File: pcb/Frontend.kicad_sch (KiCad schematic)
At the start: 382 parts, among them IC1 TS3021ILT, IC10 TS3021ILT, IC11 TS3021ILT, IC12 TS3021ILT, IC13 TS3021ILT, IC14 TS3021ILT, IC2 TS3021ILT, IC3 TS3021ILT, IC4 TS3021ILT, IC5 TS3021ILT, IC6 TS3021ILT, IC7 TS3021ILT, IC8 TS3021ILT, IC9 TS3021ILT, J1 Conn_01x05_Socket, J2 Conn_01x05_Socket, J3 Conn_01x04_Socket, J4 Conn_01x04_Socket, U1 TEA1-0505, U10 ADuM1400xRW, U11 GAQY212GS, U12 GAQY212GS, U13 GAQY212GS, U14 GAQY212GS, U15 LM4040DBZ-5, U16 DAC7311xDCK, U17 ADuM1300xRW, U18 TEA1-0505, U19 GAQY212GS, U2 GAQY212GS, U20 GAQY212GS, U21 GAQY212GS, U22 GAQY212GS, U23 GAQY212GS, U24 GAQY212GS, U25 GAQY212GS, U26 GAQY212GS, U27 ADuM1400xRW, U28 GAQY212GS, U29 GAQY212GS, U3 GAQY212GS, U30 GAQY212GS, U31 GAQY212GS, U32 LM4040DBZ-5, U33 DAC7311xDCK, U34 ADuM1300xRW, U35 TEA1-0505, U36 GAQY212GS, U37 GAQY212GS, U38 GAQY212GS, U39 GAQY212GS, U4 GAQY212GS, U40 GAQY212GS, U41 GAQY212GS, U42 ADuM1300xRW, U43 GAQY212GS, U44 GAQY212GS, U45 GAQY212GS, U46 LM4040DBZ-5, U47 DAC7311xDCK, U48 ADuM1300xRW, U49 TEA1-0505, U5 GAQY212GS, U50 GAQY212GS, U51 GAQY212GS, U52 GAQY212GS, U53 GAQY212GS, U54 GAQY212GS, U55 GAQY212GS, U56 ADuM1300xRW, U57 GAQY212GS, U58 GAQY212GS, U59 GAQY212GS, U6 GAQY212GS, U60 LM4040DBZ-5, U61 DAC7311xDCK, U62 ADuM1300xRW, U7 GAQY212GS, U8 GAQY212GS, U9 GAQY212GS

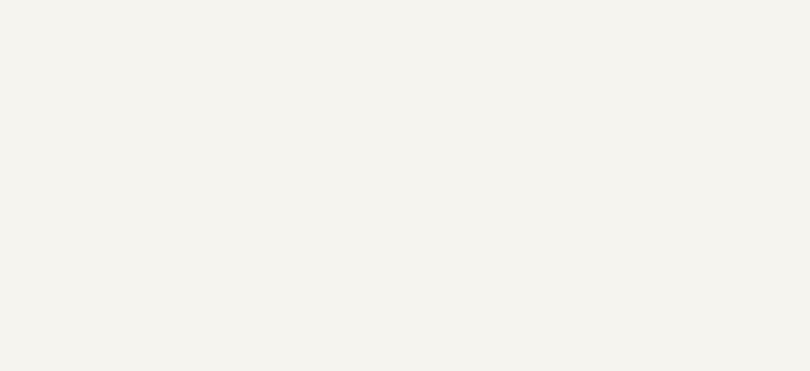
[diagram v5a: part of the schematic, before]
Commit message: Update TS3021ILT part and more routing
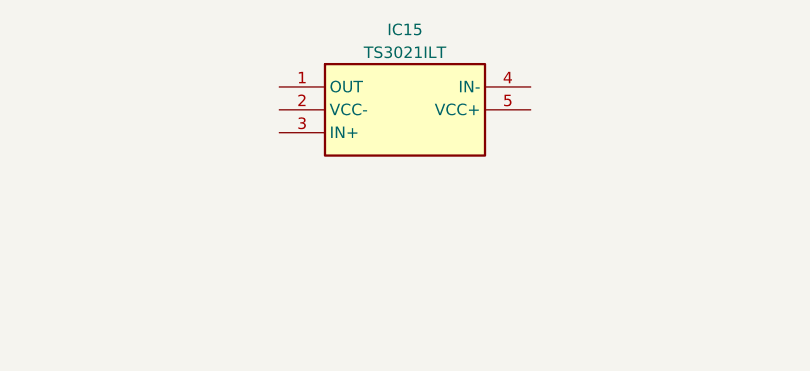
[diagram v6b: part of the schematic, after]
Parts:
- added IC15: TS3021ILT, SOT95P280X145-5N, symbol SamacSys_Parts:TS3021ILT
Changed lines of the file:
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@@
+	)
+	(symbol
+		(lib_id "SamacSys_Parts:TS3021ILT")
+		(at 457.2 -11.43 0)
+		(unit 1)
+		(exclude_from_sim no)
+		(in_bom yes)
+		(on_board yes)
+		(dnp no)
+		(fields_autoplaced yes)
+		(property "Reference" "IC15"
+			(at 471.17 -17.78 0)
+			(effects
+				(font
+					(size 1.27 1.27)
+				)
+			)
+		)
+		(property "Value" "TS3021ILT"
+			(at 471.17 -15.24 0)
+			(effects
+				(font
+					(size 1.27 1.27)
+				)
+			)
+		)
+		(property "Footprint" "SOT95P280X145-5N"
+			(at 481.33 83.49 0)
+			(effects
+				(font
+					(size 1.27 1.27)
+				)
+				(justify left top)
+				(hide yes)
+			)
+		)
+		(property "Datasheet" "https://www.st.com/resource/en/datasheet/ts3021.pdf"
+			(at 481.33 183.49 0)
+			(effects
+				(font
+					(size 1.27 1.27)
+				)
+				(justify left top)
+				(hide yes)
+			)
+		)
+		(property "Description" "Rail-to-rail 1.8 V high-speed comparator"
+			(at 457.2 -11.43 0)
+			(effects
+				(font
+					(size 1.27 1.27)
+				)
+				(hide yes)
+			)
+		)
+		(property "Height" "1.45"
+			(at 481.33 383.49 0)
+			(effects
+				(font
+					(size 1.27 1.27)
+				)
+				(justify left top)
+				(hide yes)
+			)
+		)
+		(property "TME Electronic Components Part Number" ""
+			(at 481.33 483.49 0)
+			(effects
+				(font
+					(size 1.27 1.27)
+				)
+				(justify left top)
+				(hide yes)
+			)
+		)
+		(property "TME Electronic Components Price/Stock" ""
+			(at 481.33 583.49 0)
+			(effects
+				(font
+					(size 1.27 1.27)
+				)
+				(justify left top)
+				(hide yes)
+			)
+		)
+		(property "Manufacturer_Name" "STMicroelectronics"
+			(at 481.33 683.49 0)
+			(effects
+				(font
+					(size 1.27 1.27)
+				)
+				(justify left top)
+				(hide yes)
+			)
+		)
+		(property "Manufacturer_Part_Number" "TS3021ILT"
+			(at 481.33 783.49 0)
+			(effects
+				(font
+					(size 1.27 1.27)
+				)
+				(justify left top)
+				(hide yes)
+			)
+		)
+		(pin "1"
+		)
+		(pin "3"
+		)
+		(pin "5"
+		)
+		(pin "4"
+		)
+		(pin "2"
+		)
+		(instances
+			(project ""
+				(path "/0c4edb77-9bdf-4103-be66-c5eb9940b163/92da3f15-6ca3-419e-9376-1f5f82193d40"
+					(reference "IC15")
+					(unit 1)
+				)
+			)
+		)
 	)
 	(symbol

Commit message: Update schematic, more routing
Add firmware/TSC_RangeControl.ioc (STM32CubeMX project for STM32C011F4Px). Numerous adjustments to the schematic. Update PCB files.
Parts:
- removed IC15: TS3021ILT, SOT95P280X145-5N, symbol SamacSys_Parts:TS3021ILT
- added C64, C65: 100n, Capacitor_SMD:C_0603_1608Metric, symbol Device:C
- added IC15: NCP51460SN33T1G, SOT96P237X111-3N, symbol SamacSys_Parts:NCP51460SN33T1G
- added U64: STM32C011F4Px, Package_SO:TSSOP-20_4.4x6.5mm_P0.65mm, symbol MCU_ST_STM32C0:STM32C011F4Px
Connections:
- net +5V: now also C65.1, IC15.1 (VIN)
- net GND: now also C64.2, C65.2, IC15.3 (GND), U64.5 (VSS)
- net at C48.1, C49.2, C52.2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: now also C58.2
- net at C17.1, C18.2, C21.2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: now also C28.2
- net at C1.1, C10.2, C11.2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: now also C12.2
- net at C12.1, FB10.1, U17.10 (V_{E2})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: no longer C12.2
- net at C58.1, FB29.1, U62.10 (V_{E2})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: no longer C58.2
- net at C28.1, FB17.1, U34.10 (V_{E2})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: no longer C28.2
- new net: C64.1, IC15.2 (VOUT), U64.4 (VDD)

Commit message: New range control concept
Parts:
- added C66, C67, C68, C69, C70, C71: 100n, Capacitor_SMD:C_0603_1608Metric, symbol Device:C
- added D15, D16, D17, D18: D, Diode_SMD:D_SOD-323F, symbol Device:D
- added IC16, IC17, IC18: NCP51460SN33T1G, Package_TO_SOT_SMD:SOT-23, symbol SamacSys_Parts:NCP51460SN33T1G
- added R201, R202, R203, R204: 10k, Resistor_SMD:R_0603_1608Metric, symbol Device:R
- added TP1, TP10, TP11, TP12, TP2, TP3, TP4, TP5, TP6, TP7, TP8, TP9: TestPoint, TestPoint:TestPoint_Pad_D1.0mm, symbol Connector:TestPoint
- added U65, U66, U67: STM32C011F4Px, Package_SO:TSSOP-20_4.4x6.5mm_P0.65mm, symbol MCU_ST_STM32C0:STM32C011F4Px
- IC15: footprint SOT96P237X111-3N -> Package_TO_SOT_SMD:SOT-23
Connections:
- net +5V: now also C67.1, C69.1, C71.1, IC16.1 (VIN), IC17.1 (VIN), IC18.1 (VIN)
- net CH1_IN1_R15: now also U64.8 (PA1)
- net CH1_IN1_R25: now also U64.9 (PA2)
- net CH1_IN1_R5: now also U64.7 (PA0)
- net CH1_IN2_R15: now also U64.11 (PA4)
- net CH1_IN2_R25: now also U64.12 (PA5)
- net CH1_IN2_R5: now also U64.10 (PA3)
- net CH1_IN3_R15: now also U64.14 (PA7)
- net CH1_IN3_R25: now also U64.15 (PA8)
- net CH1_IN3_R5: now also U64.13 (PA6)
- net CH1_IN4_R15: now also U64.17 (PA10/PA12)
- net CH1_IN4_R25: now also U64.20 (PB6)
- net CH1_IN4_R5: now also U64.16 (PA9/PA11)
- net CH2_IN1_R15: now also U65.8 (PA1)
- net CH2_IN1_R25: now also U65.9 (PA2)
- net CH2_IN1_R5: now also U65.7 (PA0)
- net CH2_IN2_R15: now also U65.11 (PA4)
- net CH2_IN2_R25: now also U65.12 (PA5)
- net CH2_IN2_R5: now also U65.10 (PA3)
- net CH2_IN3_R15: now also U65.14 (PA7)
- net CH2_IN3_R25: now also U65.15 (PA8)
- net CH2_IN3_R5: now also U65.13 (PA6)
- net CH2_IN4_R15: now also U65.17 (PA10/PA12)
- net CH2_IN4_R25: now also U65.20 (PB6)
- net CH2_IN4_R5: now also U65.16 (PA9/PA11)
- net CH3_IN1_R15: now also U66.8 (PA1); no longer R179.1, U53.2
- net CH3_IN1_R25: now also U66.9 (PA2); no longer R164.1, U50.2
- net CH3_IN1_R5: now also U66.7 (PA0); no longer R196.1, U59.2
- net CH3_IN2_R15: now also U66.11 (PA4); no longer R180.1, U54.2
- net CH3_IN2_R25: now also U66.12 (PA5); no longer R165.1, U51.2
- net CH3_IN2_R5: now also U66.10 (PA3); no longer R194.1, U57.2
- net CH3_IN3_R15: now also U66.14 (PA7); no longer R181.1, U55.2
- net CH3_IN3_R25: now also U66.15 (PA8); no longer R166.1, U52.2
- net CH3_IN3_R5: now also U66.13 (PA6); no longer R195.1, U58.2
- net GND: now also C66.2, C67.2, C68.2, C69.2, C70.2, C71.2, IC16.3 (GND), IC17.3 (GND), IC18.3 (GND), R201.2, R202.2, U65.5 (VSS), U66.5 (VSS), U67.5 (VSS)
- net USART_RX: now reaches U64.1 (PB7)
- net USART_RX: now also U65.1 (PB7), U66.1 (PB7), U67.1 (PB7)
- net at U64.18 (PA13): now also TP1.1
- net at U64.19 (PA14): now also TP2.1
- net at U64.2 (PC14): now also D16.1 (K)
- net at U64.3 (PC15): now also R201.1
- net at U64.6 (PF2): now also TP3.1
- new net: TP11.1, U67.18 (PA13)
- new net: D17.1 (K), U66.2 (PC14)
- new net: C68.1, IC17.2 (VOUT), R203.1, U66.4 (VDD)
- new net: TP8.1, U66.18 (PA13)
- new net: TP5.1, U65.18 (PA13)
- new net: TP6.1, U65.19 (PA14)
- new net: D15.1 (K), U65.2 (PC14)
- new net: R202.1, U65.3 (PC15)
- new net: C66.1, IC16.2 (VOUT), U65.4 (VDD)
- new net: TP4.1, U65.6 (PF2)
- new net: R203.2, U66.3 (PC15)
- new net: TP7.1, U66.6 (PF2)
- new net: C70.1, IC18.2 (VOUT), R204.1, U67.4 (VDD)
- new net: R204.2, U67.3 (PC15)
- new net: TP12.1, U67.19 (PA14)
- new net: D18.1 (K), U67.2 (PC14)
- new net: TP10.1, U67.6 (PF2)
- new net: TP9.1, U66.19 (PA14)
- new net CH4_IN1_R15: R179.1, U53.2, U67.8 (PA1)
- new net CH4_IN1_R25: R164.1, U50.2, U67.9 (PA2)
- new net CH4_IN1_R5: R196.1, U59.2, U67.7 (PA0)
- new net CH4_IN2_R15: R180.1, U54.2, U67.11 (PA4)
- new net CH4_IN2_R25: R165.1, U51.2, U67.12 (PA5)
- new net CH4_IN2_R5: R194.1, U57.2, U67.10 (PA3)
- new net CH4_IN3_R15: R181.1, U55.2, U67.14 (PA7)
- new net CH4_IN3_R25: R166.1, U52.2, U67.15 (PA8)
- new net CH4_IN3_R5: R195.1, U58.2, U67.13 (PA6)
- new net USART_TX: D15.2 (A), D16.2 (A), D17.2 (A), D18.2 (A)
- no-connect marks 0 -> 6
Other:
- moved on the sheet: C64, C65, IC15, U64
